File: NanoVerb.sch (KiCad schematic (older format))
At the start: 5 parts, among them U6 7805, U7 V53C104FP60, U8 TL084CN, U9 TL084CN

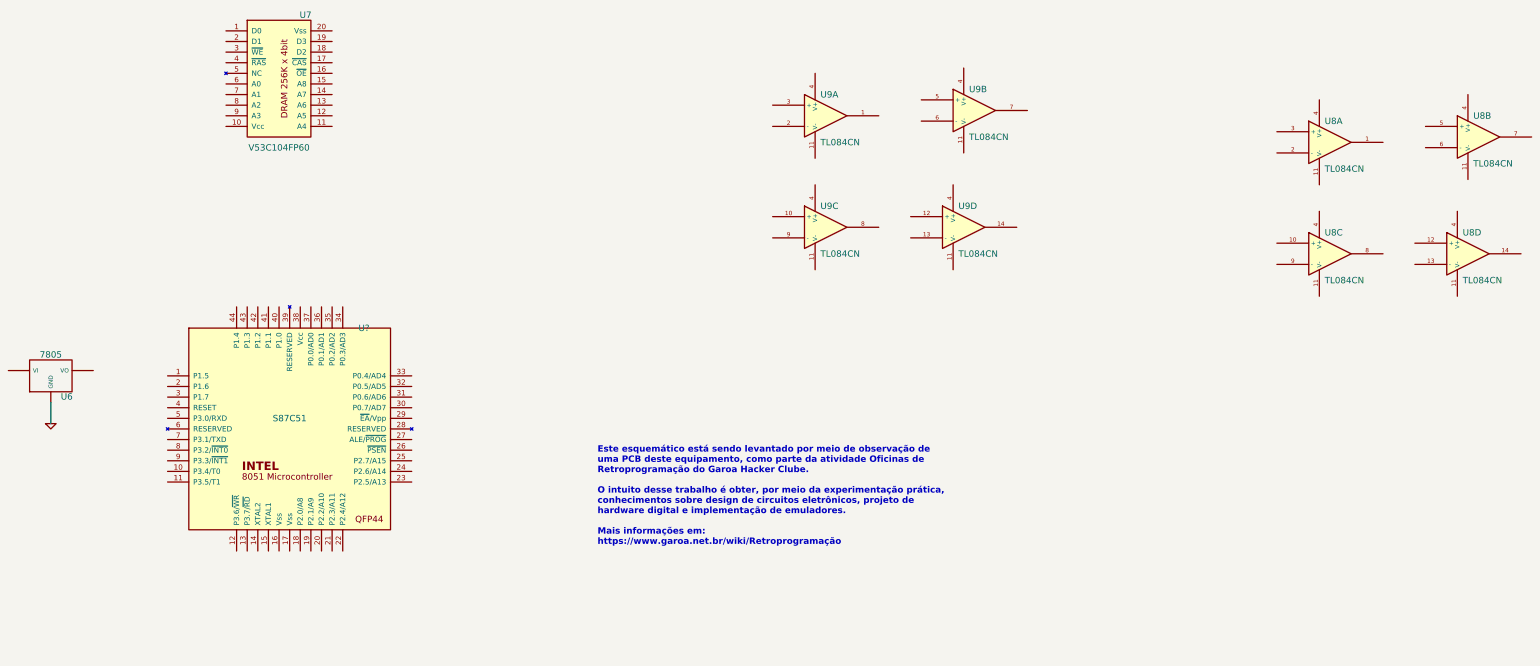
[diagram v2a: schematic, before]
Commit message: updating schematics by adding the undocumented ALESIS IC
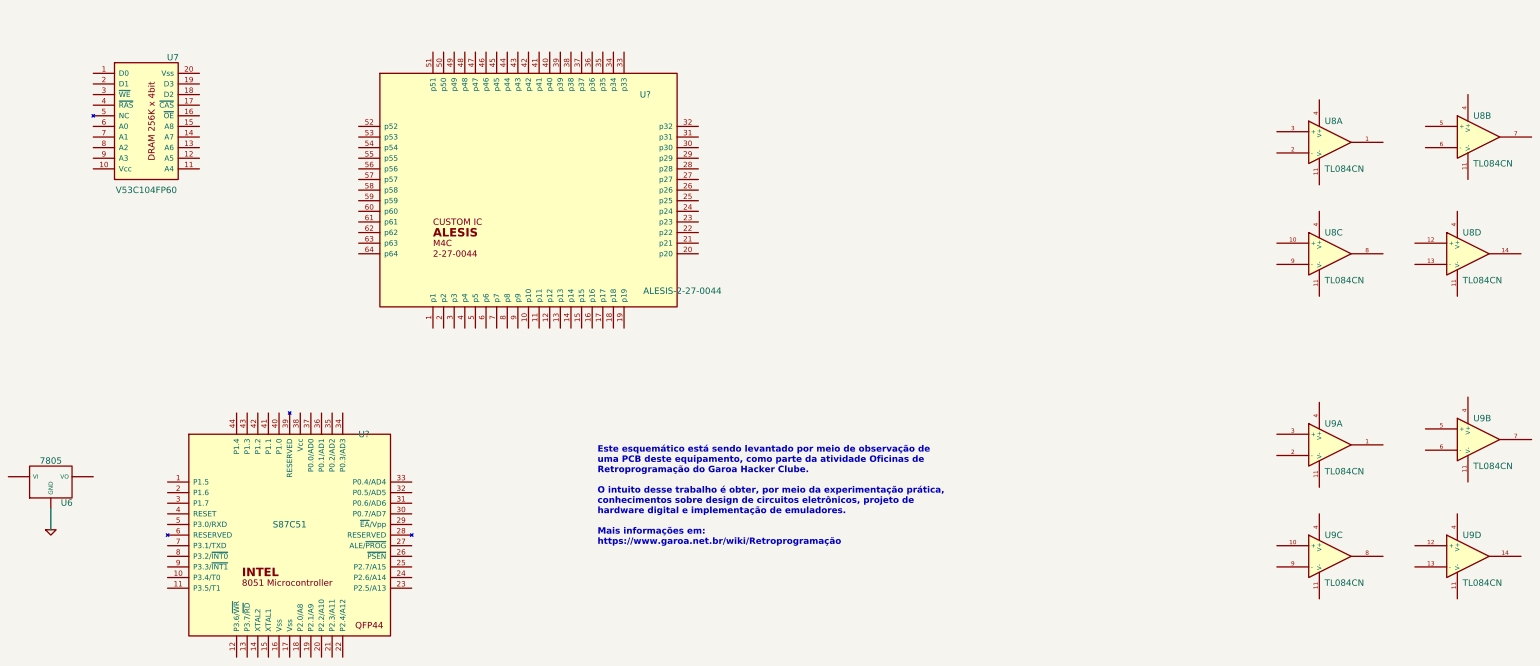
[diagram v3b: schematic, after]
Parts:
- added U?: ALESIS-2-27-0044, symbol ALESIS-2-27-0044
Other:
- moved on the sheet: U6, U7, U9A, U9B, U9C, U9D, U?
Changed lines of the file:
@@
 LIBS:tl084cn
 LIBS:v53c104fp60
+LIBS:alesis-2-27-0044
 LIBS:NanoVerb-cache
 EELAYER 25 0
@@
 L 7805 U6
 U 1 1 54A6E5DC
-P 1850 4850
-F 0 "U6" H 2000 4654 60  0000 C CNN
-F 1 "7805" H 1850 5050 60  0000 C CNN
-F 2 "" H 1850 4850 60  0000 C CNN
-F 3 "" H 1850 4850 60  0000 C CNN
-	1    1850 4850
+P 1850 5850
+F 0 "U6" H 2000 5654 60  0000 C CNN
+F 1 "7805" H 1850 6050 60  0000 C CNN
+F 2 "" H 1850 5850 60  0000 C CNN
+F 3 "" H 1850 5850 60  0000 C CNN
+	1    1850 5850
 	1    0    0    -1
 $EndComp
@@
 L GND #PWR?
 U 1 1 54A6E8E7
-P 1850 5300
-F 0 "#PWR?" H 1850 5300 30  0001 C CNN
-F 1 "GND" H 1850 5230 30  0001 C CNN
-F 2 "" H 1850 5300 60  0000 C CNN
-F 3 "" H 1850 5300 60  0000 C CNN
-	1    1850 5300
+P 1850 6300
+F 0 "#PWR?" H 1850 6300 30  0001 C CNN
+F 1 "GND" H 1850 6230 30  0001 C CNN
+F 2 "" H 1850 6300 60  0000 C CNN
+F 3 "" H 1850 6300 60  0000 C CNN
+	1    1850 6300
 	1    0    0    -1
 $EndComp
 Wire Wire Line
-	1850 5300 1850 5100
+	1850 6300 1850 6100
 $Comp
 L S87C51 U?
 U 1 1 54A6F801
-P 4100 5350
-F 0 "U?" H 4800 6300 60  0000 C CNN
-F 1 "S87C51" H 4100 5450 60  0000 C CNN
-F 2 "" H 4100 5350 60  0000 C CNN
-F 3 "" H 4100 5350 60  0000 C CNN
-	1    4100 5350
+P 4100 6350
+F 0 "U?" H 4800 7300 60  0000 C CNN
+F 1 "S87C51" H 4100 6450 60  0000 C CNN
+F 2 "" H 4100 6350 60  0000 C CNN
+F 3 "" H 4100 6350 60  0000 C CNN
+	1    4100 6350
 	1    0    0    -1
 $EndComp
@@
 L TL084CN U9
 U 1 1 54A6F65E
-P 9150 2400
-F 0 "U9" H 9100 2600 60  0000 L CNN
-F 1 "TL084CN" H 9100 2150 60  0000 L CNN
-F 2 "" H 9150 2400 60  0000 C CNN
-F 3 "" H 9150 2400 60  0000 C CNN
-	1    9150 2400
+P 13900 5500
+F 0 "U9" H 13850 5700 60  0000 L CNN
+F 1 "TL084CN" H 13850 5250 60  0000 L CNN
+F 2 "" H 13900 5500 60  0000 C CNN
+F 3 "" H 13900 5500 60  0000 C CNN
+	1    13900 5500
 	1    0    0    -1
 $EndComp
@@
 L TL084CN U9
 U 3 1 54A6F6C1
-P 9150 3450
-F 0 "U9" H 9100 3650 60  0000 L CNN
-F 1 "TL084CN" H 9100 3200 60  0000 L CNN
-F 2 "" H 9150 3450 60  0000 C CNN
-F 3 "" H 9150 3450 60  0000 C CNN
-	3    9150 3450
+P 13900 6550
+F 0 "U9" H 13850 6750 60  0000 L CNN
+F 1 "TL084CN" H 13850 6300 60  0000 L CNN
+F 2 "" H 13900 6550 60  0000 C CNN
+F 3 "" H 13900 6550 60  0000 C CNN
+	3    13900 6550
 	1    0    0    -1
 $EndComp
@@
 L TL084CN U9
 U 4 1 54A6F6FF
-P 10450 3450
-F 0 "U9" H 10400 3650 60  0000 L CNN
-F 1 "TL084CN" H 10400 3200 60  0000 L CNN
-F 2 "" H 10450 3450 60  0000 C CNN
-F 3 "" H 10450 3450 60  0000 C CNN
-	4    10450 3450
+P 15200 6550
+F 0 "U9" H 15150 6750 60  0000 L CNN
+F 1 "TL084CN" H 15150 6300 60  0000 L CNN
+F 2 "" H 15200 6550 60  0000 C CNN
+F 3 "" H 15200 6550 60  0000 C CNN
+	4    15200 6550
 	1    0    0    -1
 $EndComp
@@
 L TL084CN U9
 U 2 1 54A6F73C
-P 10550 2350
-F 0 "U9" H 10500 2550 60  0000 L CNN
-F 1 "TL084CN" H 10500 2100 60  0000 L CNN
-F 2 "" H 10550 2350 60  0000 C CNN
-F 3 "" H 10550 2350 60  0000 C CNN
-	2    10550 2350
+P 15300 5450
+F 0 "U9" H 15250 5650 60  0000 L CNN
+F 1 "TL084CN" H 15250 5200 60  0000 L CNN
+F 2 "" H 15300 5450 60  0000 C CNN
+F 3 "" H 15300 5450 60  0000 C CNN
+	2    15300 5450
 	1    0    0    -1
 $EndComp
@@
 L V53C104FP60 U7
 U 1 1 54A70A30
-P 4000 2050
-F 0 "U7" H 4250 2650 60  0000 C CNN
-F 1 "V53C104FP60" H 4000 1400 60  0000 C CNN
-F 2 "" H 4000 2200 60  0000 C CNN
-F 3 "" H 4000 2200 60  0000 C CNN
-	1    4000 2050
+P 2750 2450
+F 0 "U7" H 3000 3050 60  0000 C CNN
+F 1 "V53C104FP60" H 2750 1800 60  0000 C CNN
+F 2 "" H 2750 2600 60  0000 C CNN
+F 3 "" H 2750 2600 60  0000 C CNN
+	1    2750 2450
 	1    0    0    -1
 $EndComp
+$Comp
+L ALESIS-2-27-0044 U?
+U 1 1 54A72216
+P 6350 3750
+F 0 "U?" H 7450 5300 60  0000 C CNN
+F 1 "ALESIS-2-27-0044" H 7800 3450 60  0000 C CNN
+F 2 "" H 5750 3550 60  0000 C CNN
+F 3 "" H 5750 3550 60  0000 C CNN
+	1    6350 3750
+	1    0    0    -1
+$EndComp

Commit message: Tracing some bus signals between the microcontroler and the custom ALESIS IC.
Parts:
- gave numbers to parts that had none: 2
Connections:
- net labels added: ADDRESS_LATCH, MCU_RESET, MCU_XTAL1, P0.0, P0.1, P0.2, P0.3, P0.4, P0.5, P0.6, P0.7, ~MCU_RD, ~MCU_WR
- wire segments 1 -> 29
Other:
- moved on the sheet: U1, U2, U6, U7, U8A, U8B, U8C, U8D, U9A, U9B, U9C, U9D

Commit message: updating schematics drawing and some IC symbols
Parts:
- added C34, C35: C, symbol C
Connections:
- net labels added: AD0, AD1, AD2, AD3, AD4, AD5, AD6, AD7, VCC
- net labels removed: P0.0, P0.1, P0.2, P0.3, P0.4, P0.5, P0.6, P0.7
- wire segments 29 -> 48
- no-connect marks 0 -> 10
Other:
- note added: "(?)"
- note added: "(GND?)"
- note added: "There's a solder blob shorting pins 20 and 21.\nIt seems to have been caused by overheat in the 7805 chip nearby."
- moved on the sheet: U1, U2

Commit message: Mapping the data and address bus between the ALESIS custom IC and the DRAM chip.
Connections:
- net GND: now also U7.16 (~OE), U7.20 (Vss)
- net VCC: now also U7.10 (Vcc)
- net RAM_D0: now reaches U7.1 (D0)
- net RAM_D0: now also U2.50 (p50)
- net RAM_A4: now reaches U7.11 (A4)
- net RAM_A4: now also U2.34 (p34)
- net RAM_A5: now reaches U7.12 (A5)
- net RAM_A5: now also U2.35 (p35)
- net RAM_A6: now reaches U7.13 (A6)
- net RAM_A6: now also U2.37 (p37)
- net RAM_A7: now reaches U7.14 (A7)
- net RAM_A7: now also U2.39 (p39)
- net RAM_A8: now reaches U7.15 (A8)
- net RAM_A8: now also U2.41 (p41)
- net ~RAM_CAS: now reaches U7.17 (~CAS)
- net ~RAM_CAS: now also U2.43 (p43)
- net RAM_D2: now reaches U7.18 (D2)
- net RAM_D2: now also U2.47 (p47)
- net RAM_D3: now reaches U7.19 (D3)
- net RAM_D3: now also U2.46 (p46)
- net RAM_D1: now reaches U7.2 (D1)
- net RAM_D1: now also U2.49 (p49)
- net ~RAM_WE: now reaches U7.3 (~WE)
- net ~RAM_WE: now also U2.45 (p45)
- net ~RAM_RAS: now reaches U7.4 (~RAS)
- net ~RAM_RAS: now also U2.44 (p44)
- net RAM_A0: now reaches U7.6 (A0)
- net RAM_A0: now also U2.42 (p42)
- net RAM_A1: now reaches U7.7 (A1)
- net RAM_A1: now also U2.40 (p40)
- net RAM_A2: now reaches U7.8 (A2)
- net RAM_A2: now also U2.38 (p38)
- net RAM_A3: now reaches U7.9 (A3)
- net RAM_A3: now also U2.36 (p36)
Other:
- moved on the sheet: U7

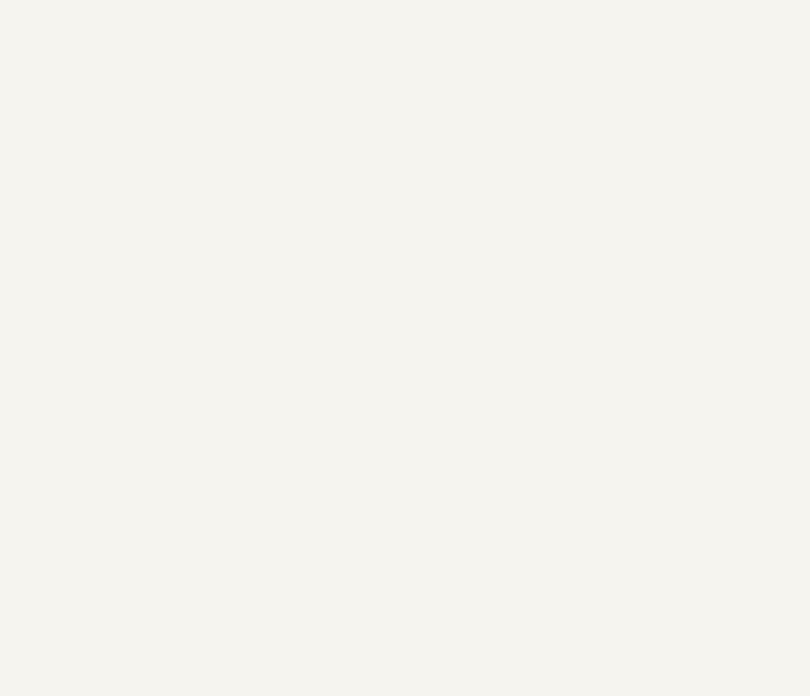
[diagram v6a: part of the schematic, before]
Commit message: Schematics symbol for the PHILIPS ADC used in the Alesis NanoVerb.
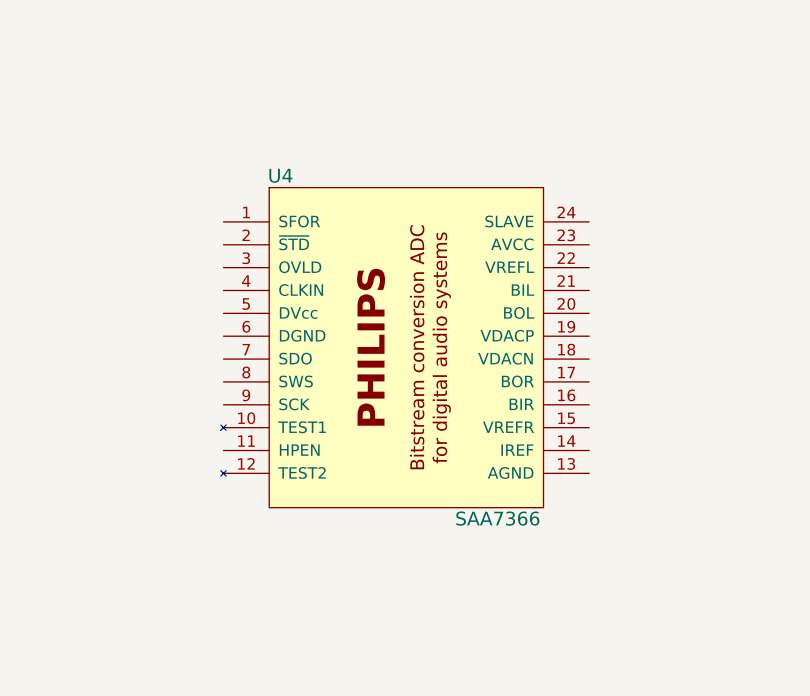
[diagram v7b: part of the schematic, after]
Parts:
- added U4: SAA7366, symbol SAA7366
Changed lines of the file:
@@
 LIBS:v53c104fp60
 LIBS:alesis-2-27-0044
+LIBS:saa7366
 LIBS:NanoVerb-cache
 EELAYER 25 0
@@
 Text Label 7250 4450 3    60   Italic 0
 RAM_A4
+$Comp
+L SAA7366 U4
+U 1 1 54A991DF
+P 12750 3800
+F 0 "U4" H 12200 4550 60  0000 C CNN
+F 1 "SAA7366" H 13150 3050 60  0000 C CNN
+F 2 "" H 12950 3350 60  0000 C CNN
+F 3 "" H 12950 3350 60  0000 C CNN
+	1    12750 3800
+	1    0    0    -1
+$EndComp
 $EndSCHEMATC
